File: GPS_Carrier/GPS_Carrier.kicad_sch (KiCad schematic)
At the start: 21 parts, among them J1 Conn_01x01_Pin, J10 Conn_01x01_Pin, J11 Conn_01x01_Pin, J2 Conn_01x01_Pin, J3 Conn_01x01_Pin, J4 Conn_01x01_Pin, J5 Conn_01x01_Pin, J6 Conn_01x01_Pin, J7 Conn_01x01_Pin, J8 Conn_01x01_Pin, J9 Conn_01x01_Pin, U1 ATGM336H-5N31, U2 AT2659, U3 AMS1117-3.3_C347222, U4 BWU.FL-IPEX1

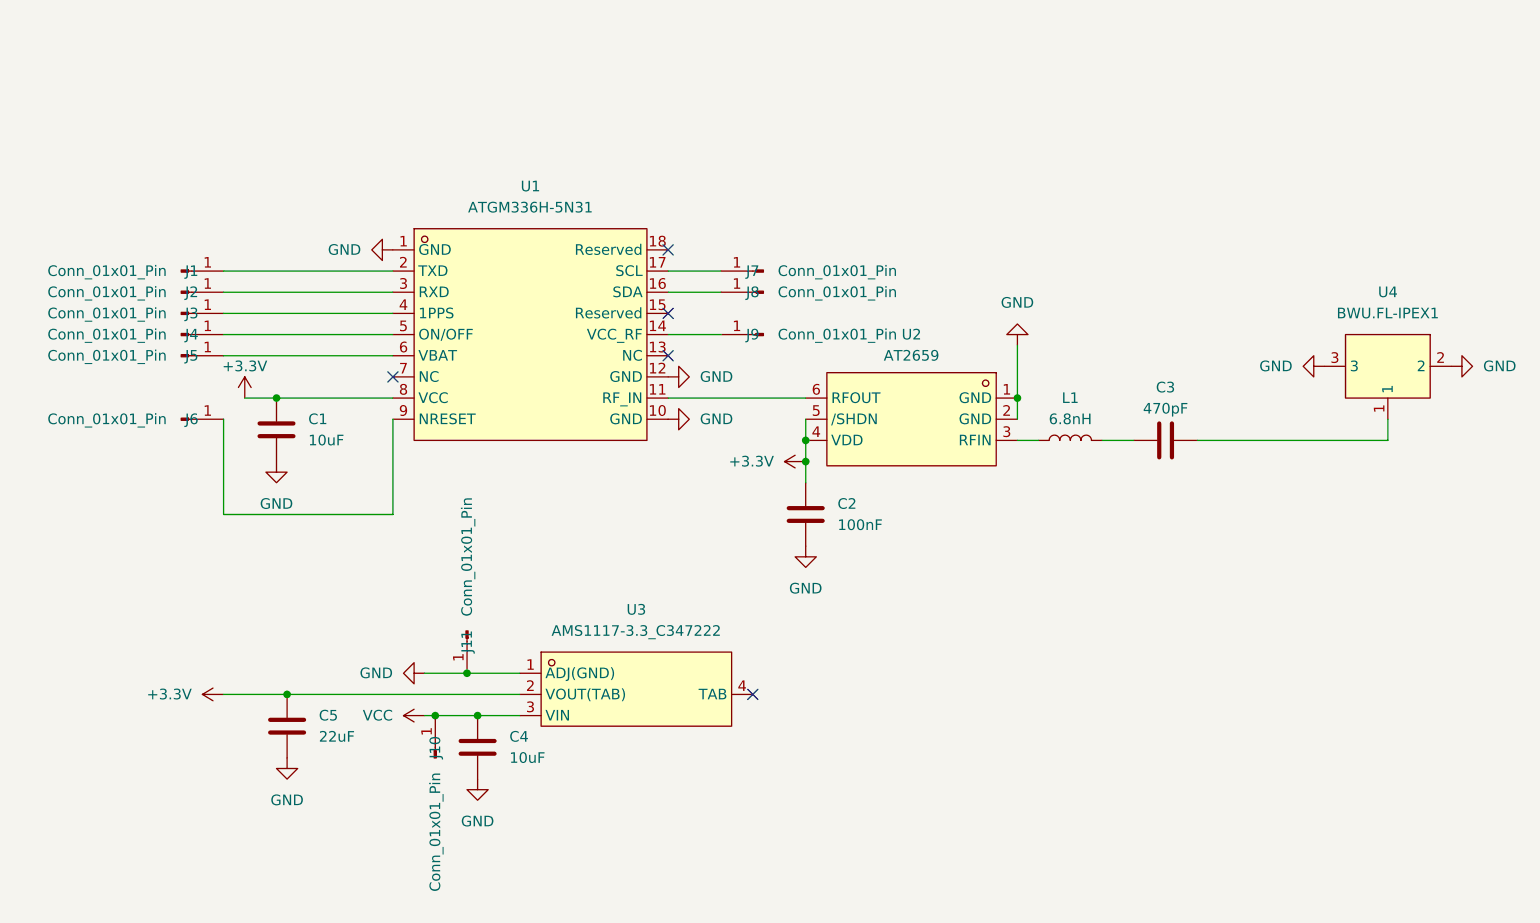
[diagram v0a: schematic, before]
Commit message: RTC and GPS Breakouts Finished
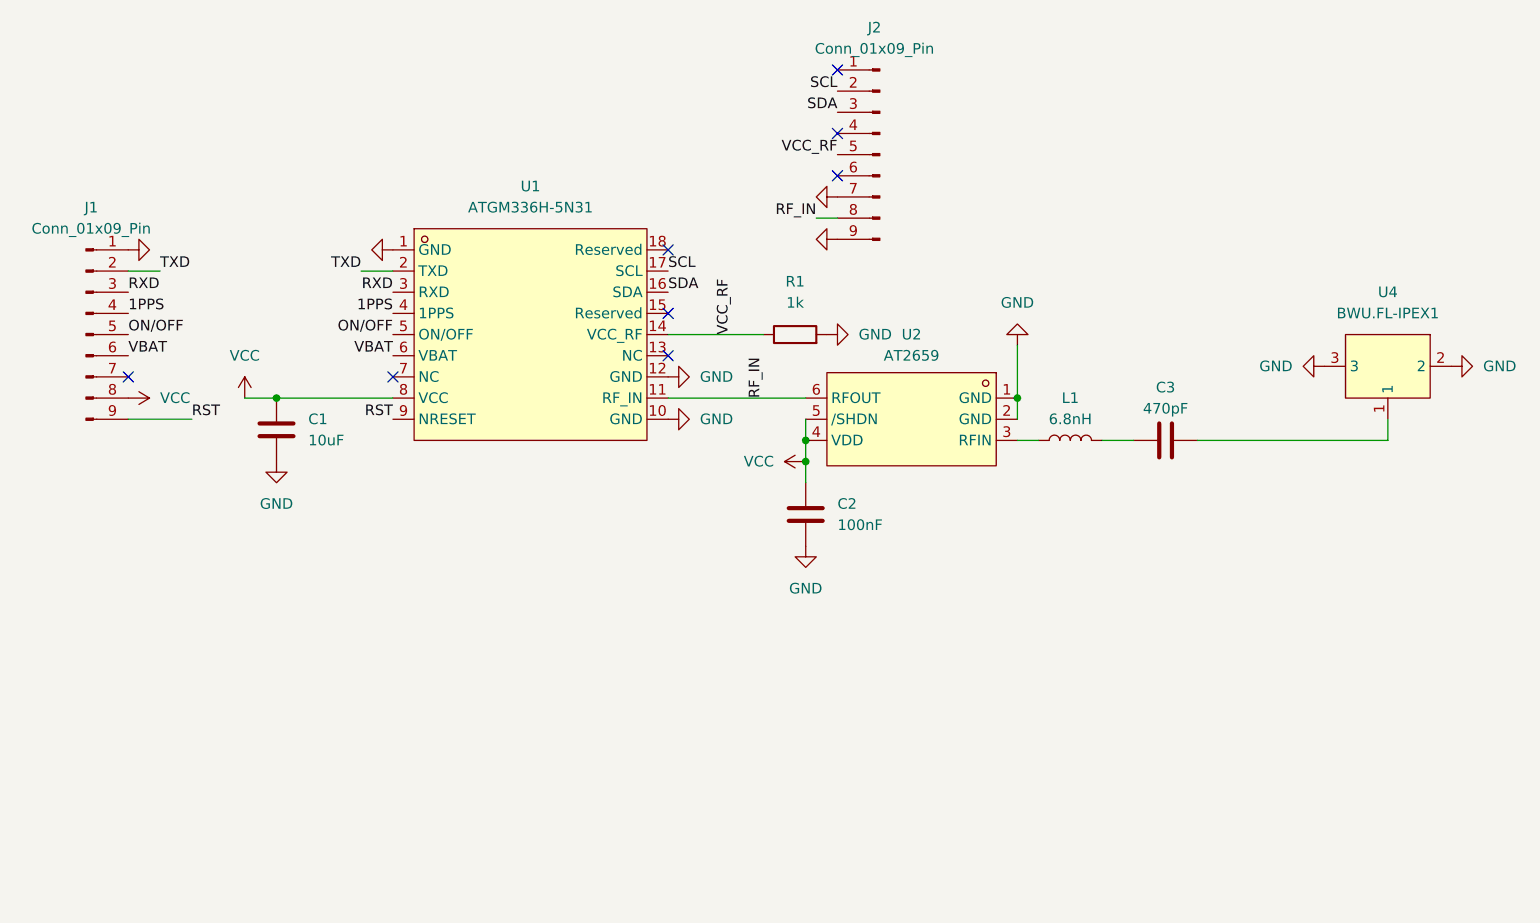
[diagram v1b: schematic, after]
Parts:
- removed C4: 10uF, Capacitor_SMD:C_0402_1005Metric, symbol Device:C
- removed C5: 22uF, Capacitor_SMD:C_0805_2012Metric, symbol Device:C
- removed J1, J10, J11, J2, J3, J4, J5, J6, J7, J8, J9: Conn_01x01_Pin, Connector_Wire:SolderWire-0.75sqmm_1x01_D1.25mm_OD2.3mm, symbol Connector:Conn_01x01_Pin
- removed U3: AMS1117-3.3_C347222, PARTS:SOT-223-4_L6.5-W3.5-P2.30-LS7.0-BR, symbol PARTS:AMS1117-3.3_C347222
- added J1, J2: Conn_01x09_Pin, Connector_PinHeader_2.54mm:PinHeader_1x09_P2.54mm_Vertical, symbol Connector:Conn_01x09_Pin
- added R1: 1k, Resistor_SMD:R_0402_1005Metric, symbol Device:R
- C2: footprint Capacitor_SMD:C_1206_3216Metric -> Capacitor_SMD:C_0402_1005Metric; LCSC Part C3839854 -> (none)
- C3: footprint Capacitor_SMD:C_1206_3216Metric -> Capacitor_SMD:C_0402_1005Metric; LCSC Part C3900342 -> (none)
- U1: footprint PARTS:RA_08H-BREAKOUT -> PARTS:GPSM-SMD_ATGM336H-TR; LCSC Part (none) -> C90770
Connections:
- net +3.3V is gone; now on net VCC: C1.1, C2.1, U1.8 (VCC), U2.4 (VDD), U2.5 (/SHDN)
- net GND: now also J1.1 (Pin_1), J2.7 (Pin_7), J2.9 (Pin_9), R1.2
- net VCC: now also J1.8 (Pin_8)
- net VCC_RF: now reaches U1.14 (VCC_RF)
- net VCC_RF: now also J2.5 (Pin_5), R1.1
- net TXD: now reaches U1.2 (TXD)
- net TXD: now also J1.2 (Pin_2)
- net RF_IN: now reaches U1.11 (RF_IN), U2.6 (RFOUT)
- net RF_IN: now also J2.8 (Pin_8)
- net SDA: now reaches U1.16 (SDA)
- net SDA: now also J2.3 (Pin_3)
- net SCL: now reaches U1.17 (SCL)
- net SCL: now also J2.2 (Pin_2)
- net RXD: now reaches U1.3 (RXD)
- net RXD: now also J1.3 (Pin_3)
- net 1PPS: now reaches U1.4 (1PPS)
- net 1PPS: now also J1.4 (Pin_4)
- net ON/OFF: now reaches U1.5 (ON/OFF)
- net ON/OFF: now also J1.5 (Pin_5)
- net VBAT: now reaches U1.6 (VBAT)
- net VBAT: now also J1.6 (Pin_6)
- net RST: now reaches U1.9 (NRESET)
- net RST: now also J1.9 (Pin_9)
- no-connect marks 5 -> 8
